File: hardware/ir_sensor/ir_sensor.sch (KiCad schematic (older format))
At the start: 5 parts

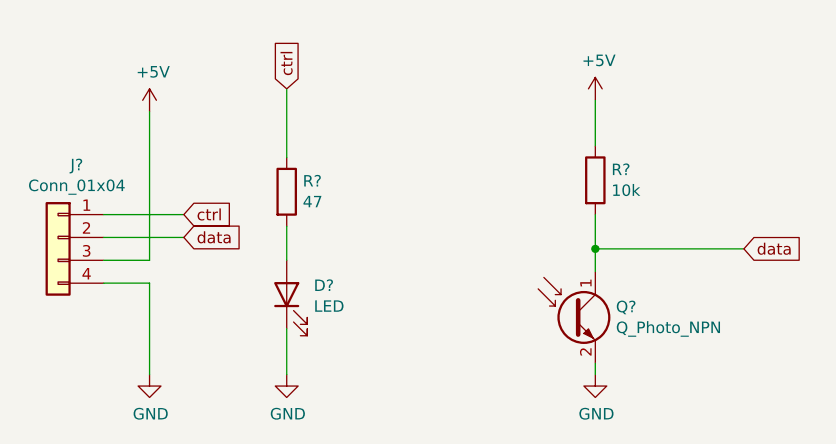
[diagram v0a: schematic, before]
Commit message: Add IR sensor/transmitter
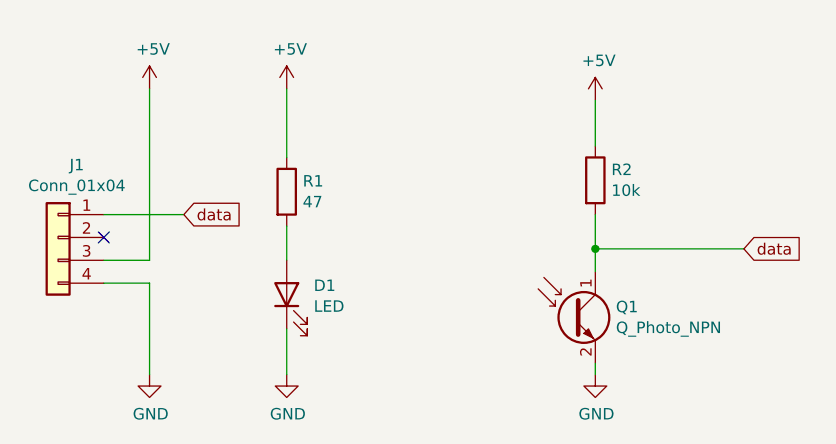
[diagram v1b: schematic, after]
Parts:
- D1: renamed from D?; footprint (none) -> LED_THT:LED_D5.0mm
- gave numbers to parts that had none: 4
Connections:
- net +5V: now also R1.1
- net data: now also J1.1 (Pin_1); no longer J1.2 (Pin_2)
- removed net ctrl: J1.1 (Pin_1), R1.1
- no-connect marks 0 -> 1
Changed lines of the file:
@@
 $EndDescr
 $Comp
-L power:GND #PWR?
+L power:GND #PWR04
 U 1 1 61058F2A
 P 1900 4700
-F 0 "#PWR?" H 1900 4450 50  0001 C CNN
+F 0 "#PWR04" H 1900 4450 50  0001 C CNN
 F 1 "GND" H 1905 4527 50  0000 C CNN
 F 2 "" H 1900 4700 50  0001 C CNN
@@
 $EndComp
 $Comp
-L Device:R R?
+L Device:R R1
 U 1 1 6105926D
 P 1900 3900
-F 0 "R?" H 1970 3946 50  0000 L CNN
+F 0 "R1" H 1970 3946 50  0000 L CNN
 F 1 "47" H 1970 3855 50  0000 L CNN
 F 2 "Resistor_THT:R_Box_L13.0mm_W4.0mm_P9.00mm" V 1830 3900 50  0001 C CNN
@@
 $EndComp
 $Comp
-L Device:LED D?
+L Device:LED D1
 U 1 1 6105A46A
 P 1900 4350
-F 0 "D?" V 1939 4232 50  0000 R CNN
+F 0 "D1" V 1939 4232 50  0000 R CNN
 F 1 "LED" V 1848 4232 50  0000 R CNN
-F 2 "" H 1900 4350 50  0001 C CNN
-F 3 "~" H 1900 4350 50  0001 C CNN
+F 2 "LED_THT:LED_D5.0mm" H 1900 4350 50  0001 C CNN
+F 3 "https://docs.rs-online.com/d7e2/0900766b80e1b0e4.pdf" H 1900 4350 50  0001 C CNN
 	1    1900 4350
 	0    -1   -1   0
@@
 	1900 4200 1900 4050
 $Comp
-L power:+5V #PWR?
+L power:+5V #PWR05
 U 1 1 6105D32C
 P 3250 3500
-F 0 "#PWR?" H 3250 3350 50  0001 C CNN
+F 0 "#PWR05" H 3250 3350 50  0001 C CNN
 F 1 "+5V" H 3265 3673 50  0000 C CNN
 F 2 "" H 3250 3500 50  0001 C CNN
@@
 $EndComp
 $Comp
-L Device:R R?
+L Device:R R2
 U 1 1 6105D332
 P 3250 3850
-F 0 "R?" H 3320 3896 50  0000 L CNN
+F 0 "R2" H 3320 3896 50  0000 L CNN
 F 1 "10k" H 3320 3805 50  0000 L CNN
 F 2 "Resistor_THT:R_Box_L13.0mm_W4.0mm_P9.00mm" V 3180 3850 50  0001 C CNN
@@
 	3250 3700 3250 3500
 $Comp
-L power:GND #PWR?
+L power:GND #PWR06
 U 1 1 6105D3A5
 P 3250 4700
-F 0 "#PWR?" H 3250 4450 50  0001 C CNN
+F 0 "#PWR06" H 3250 4450 50  0001 C CNN
 F 1 "GND" H 3255 4527 50  0000 C CNN
 F 2 "" H 3250 4700 50  0001 C CNN
@@
 $EndComp
 $Comp
-L Device:Q_Photo_NPN Q?
+L Device:Q_Photo_NPN Q1
 U 1 1 6105E56E
 P 3150 4450
-F 0 "Q?" H 3340 4496 50  0000 L CNN
+F 0 "Q1" H 3340 4496 50  0000 L CNN
 F 1 "Q_Photo_NPN" H 3340 4405 50  0000 L CNN
 F 2 "LED_THT:OP505A" H 3350 4550 50  0001 C CNN
@@
 	3250 4150 3250 4250
 $Comp
-L Connector_Generic:Conn_01x04 J?
+L Connector_Generic:Conn_01x04 J1
 U 1 1 61059BBB
 P 900 4100
-F 0 "J?" H 818 4417 50  0000 C CNN
+F 0 "J1" H 818 4417 50  0000 C CNN
 F 1 "Conn_01x04" H 818 4326 50  0000 C CNN
 F 2 "Connector_JST:JST_XH_B4B-XH-A_1x04_P2.50mm_Vertical" H 900 4100 50  0001 C CNN
@@
 $EndComp
 $Comp
-L power:GND #PWR?
+L power:GND #PWR02
 U 1 1 6105B3FB
 P 1300 4700
-F 0 "#PWR?" H 1300 4450 50  0001 C CNN
+F 0 "#PWR02" H 1300 4450 50  0001 C CNN
 F 1 "GND" H 1305 4527 50  0000 C CNN
 F 2 "" H 1300 4700 50  0001 C CNN
@@
 Wire Wire Line
 	1100 4200 1300 4200
-Text GLabel 1900 3450 1    50   Input ~ 0
-ctrl
 Wire Wire Line
 	1900 3450 1900 3750
 Text GLabel 1450 4000 2    50   Input ~ 0
-ctrl
-Text GLabel 1450 4100 2    50   Input ~ 0
 data
 Wire Wire Line
 	1100 4000 1450 4000
-Wire Wire Line
-	1100 4100 1450 4100
-Wire Wire Line
-	1300 4200 1300 3550
 $Comp
-L power:+5V #PWR?
+L power:+5V #PWR01
 U 1 1 6105B8D1
-P 1300 3550
-F 0 "#PWR?" H 1300 3400 50  0001 C CNN
-F 1 "+5V" H 1315 3723 50  0000 C CNN
-F 2 "" H 1300 3550 50  0001 C CNN
-F 3 "" H 1300 3550 50  0001 C CNN
-	1    1300 3550
+P 1300 3450
+F 0 "#PWR01" H 1300 3300 50  0001 C CNN
+F 1 "+5V" H 1315 3623 50  0000 C CNN
+F 2 "" H 1300 3450 50  0001 C CNN
+F 3 "" H 1300 3450 50  0001 C CNN
+	1    1300 3450
 	1    0    0    -1
 $EndComp
+NoConn ~ 1100 4100
+$Comp
+L power:+5V #PWR03
+U 1 1 6106B706
+P 1900 3450
+F 0 "#PWR03" H 1900 3300 50  0001 C CNN
+F 1 "+5V" H 1915 3623 50  0000 C CNN
+F 2 "" H 1900 3450 50  0001 C CNN
+F 3 "" H 1900 3450 50  0001 C CNN
+	1    1900 3450
+	1    0    0    -1
+$EndComp
+Wire Wire Line
+	1300 3450 1300 4200
 $EndSCHEMATC
